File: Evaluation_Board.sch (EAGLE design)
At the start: 38 parts, among them IC1 MEGA32-A, IC2 FT232RL, IC3 317EMP, J1 DCJ0202, Q1 16 MHz

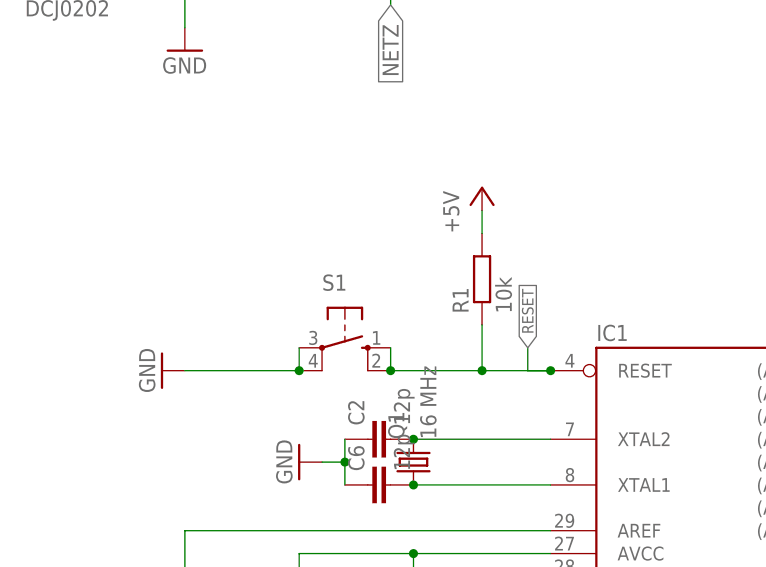
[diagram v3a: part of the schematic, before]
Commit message: Added measures. Placed all silk screen prints. PCB text now on bottom layer.
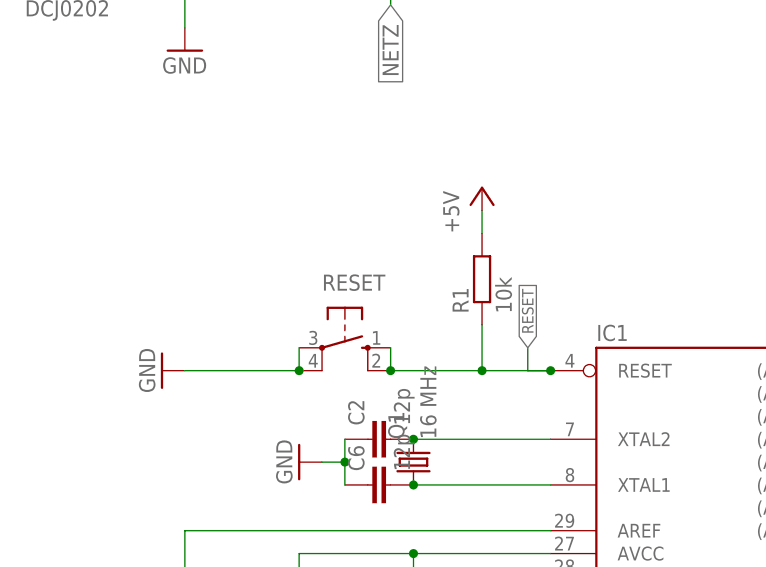
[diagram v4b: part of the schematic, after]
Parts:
- renumbered S1 to RESET
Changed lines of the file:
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@@
 <part name="R1" library="rcl" deviceset="R-EU_" device="R0805" value="10k"/>
 <part name="R2" library="rcl" deviceset="R-EU_" device="R0805" value="1k"/>
-<part name="S1" library="switch-omron" deviceset="10-XX" device=""/>
+<part name="RESET" library="switch-omron" deviceset="10-XX" device=""/>
 <part name="SUPPLY2" library="supply1" deviceset="GND" device=""/>
 <part name="C3" library="rcl" deviceset="C-EU" device="C0805" value="100n"/>
@@
 <instance part="R1" gate="G$1" x="78.74" y="208.28" rot="R90"/>
 <instance part="R2" gate="G$1" x="271.78" y="223.52"/>
-<instance part="S1" gate="1" x="63.5" y="200.66" rot="R270"/>
+<instance part="RESET" gate="1" x="63.5" y="200.66" rot="R270"/>
 <instance part="SUPPLY2" gate="1" x="43.18" y="198.12" rot="R270"/>
 <instance part="C3" gate="G$1" x="66.04" y="137.16" rot="R180"/>
@@
 <wire x1="78.74" y1="203.2" x2="78.74" y2="198.12" width="0.1524" layer="91"/>
 <wire x1="78.74" y1="198.12" x2="86.36" y2="198.12" width="0.1524" layer="91"/>
-<pinref part="S1" gate="1" pin="S1"/>
+<pinref part="RESET" gate="1" pin="S1"/>
 <wire x1="78.74" y1="198.12" x2="68.58" y2="198.12" width="0.1524" layer="91"/>
 <junction x="78.74" y="198.12"/>
@@
 <junction x="86.36" y="198.12"/>
 <label x="83.82" y="200.66" size="1.27" layer="95" rot="R90" xref="yes"/>
-<pinref part="S1" gate="1" pin="S"/>
+<pinref part="RESET" gate="1" pin="S"/>
 <wire x1="68.58" y1="200.66" x2="68.58" y2="198.12" width="0.1524" layer="91"/>
 <junction x="68.58" y="198.12"/>
@@
 <segment>
 <pinref part="SUPPLY2" gate="1" pin="GND"/>
-<pinref part="S1" gate="1" pin="P1"/>
+<pinref part="RESET" gate="1" pin="P1"/>
 <wire x1="45.72" y1="198.12" x2="58.42" y2="198.12" width="0.1524" layer="91"/>
-<pinref part="S1" gate="1" pin="P"/>
+<pinref part="RESET" gate="1" pin="P"/>
 <wire x1="58.42" y1="200.66" x2="58.42" y2="198.12" width="0.1524" layer="91"/>
 <junction x="58.42" y="198.12"/>
